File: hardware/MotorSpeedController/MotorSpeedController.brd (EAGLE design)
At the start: 51.2 x 29.2 mm, 49 parts, among them IC1 MIC5219 5V, IC2 ATMEGA32U4-AU, J1 POWER, J2 MOTOR, J3 USB MICRO, J4 I2C, J5 PROG, Q1 16MHz

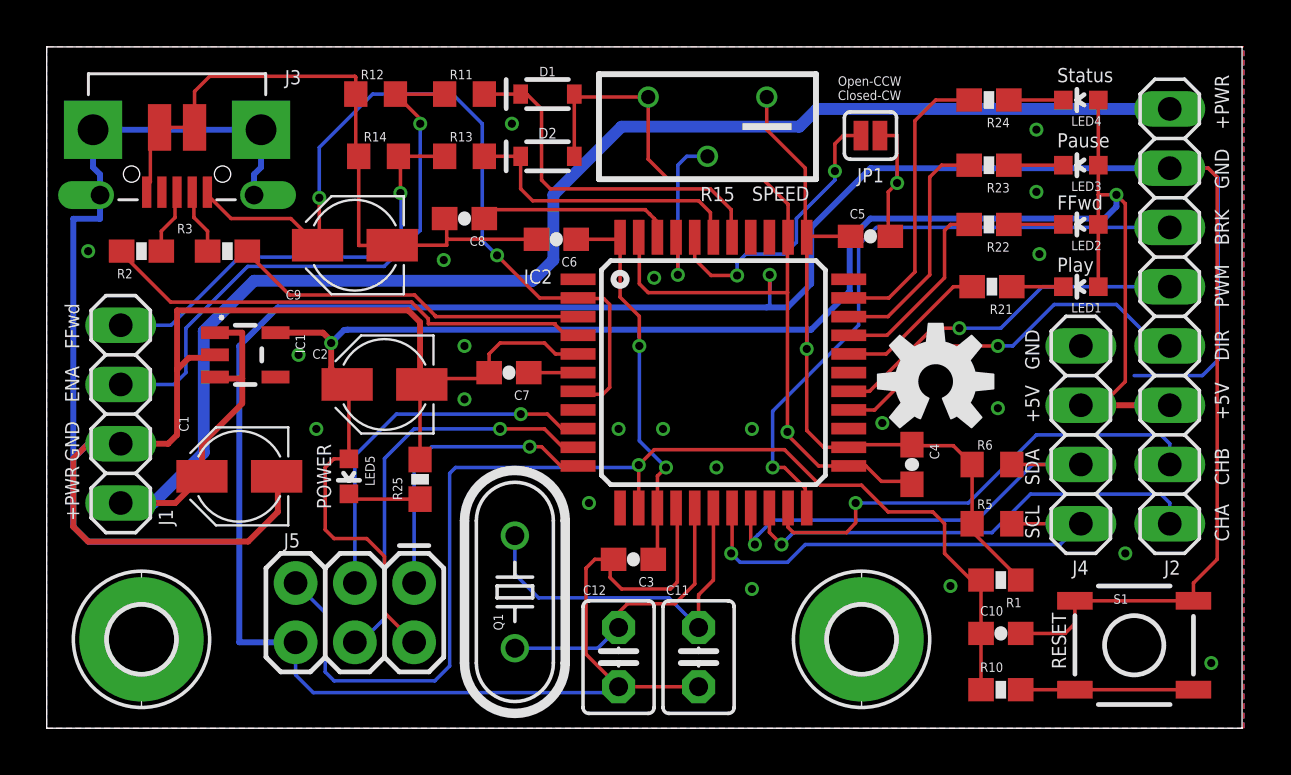
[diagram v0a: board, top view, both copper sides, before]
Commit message: Add I2C interrupt/IO.
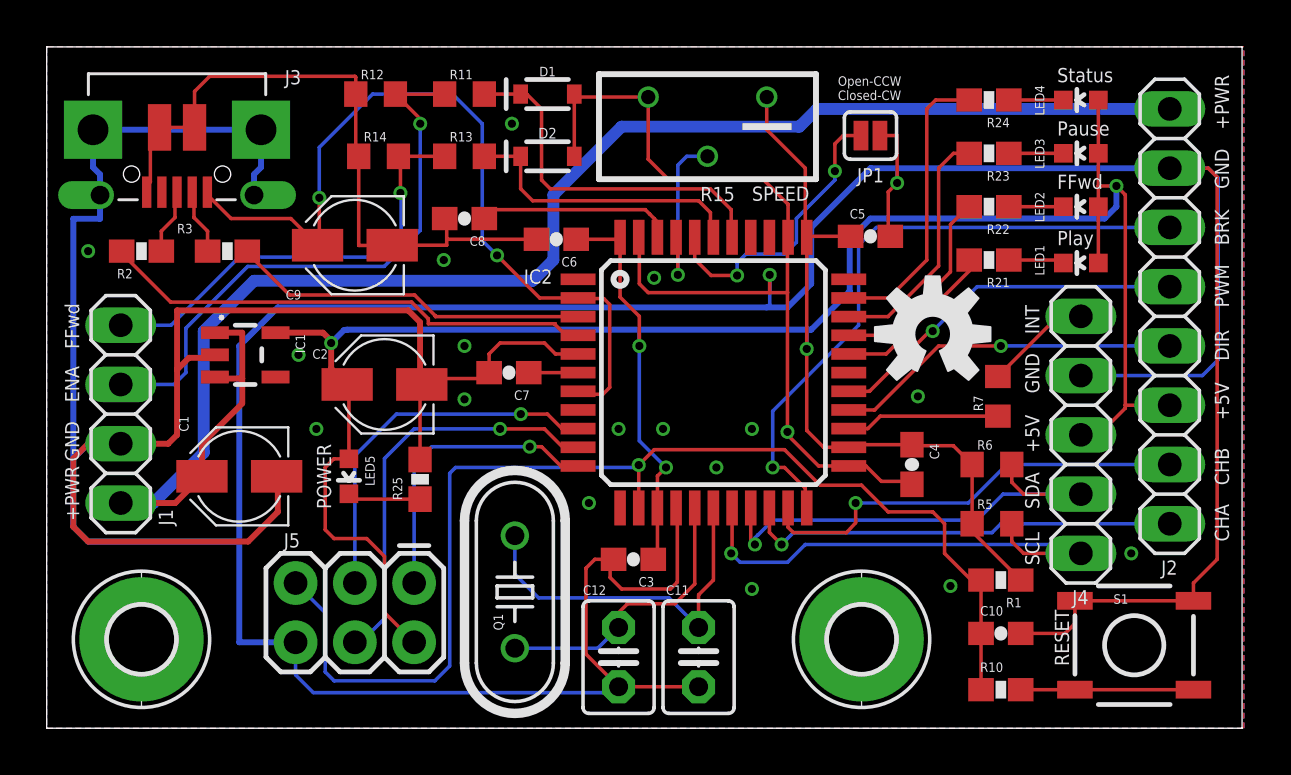
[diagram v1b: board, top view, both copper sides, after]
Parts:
- added R7: 4.7k, rcl:R0603
- J4: device pinhead:1X04 -> pinhead:1X05
- moved U$1 2.04 mm to (38.0, 16.9)
- moved U$2 1.17 mm to (42.9, 1.52)
- moved R21 1.15 mm to (40.4, 20.1)
- moved LED1 1.02 mm to (44.3, 19.9)
- moved LED2 0.76 mm to (44.3, 22.4)
- moved R22 0.76 mm to (40.4, 22.4)
- moved LED3 0.51 mm to (44.3, 24.6)
- moved R23 0.51 mm to (40.4, 24.6)
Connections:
- new net INT: IC2.25, R7.1
- new net N$8: J4.5, R7.2
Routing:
- net INT: track 0.00 -> 6.61 mm
- net N$8: track 0.00 -> 4.62 mm
- net GND: track 303.5 -> 305.2 mm, vias 25 -> 20
- net CHB: track 20.6 -> 19.0 mm
- net CHA: track 20.4 -> 18.8 mm
- net DIR: track 16.4 -> 14.9 mm
- net +5V: track 128.8 -> 127.8 mm
- net SCL: track 20.7 -> 21.5 mm
- net LED1: track 6.48 -> 7.10 mm
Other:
- board text added: "INT"

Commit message: Change footprints to match ordered parts. Put some space between crystal and ICSP. Increase clearance on PWR trace.
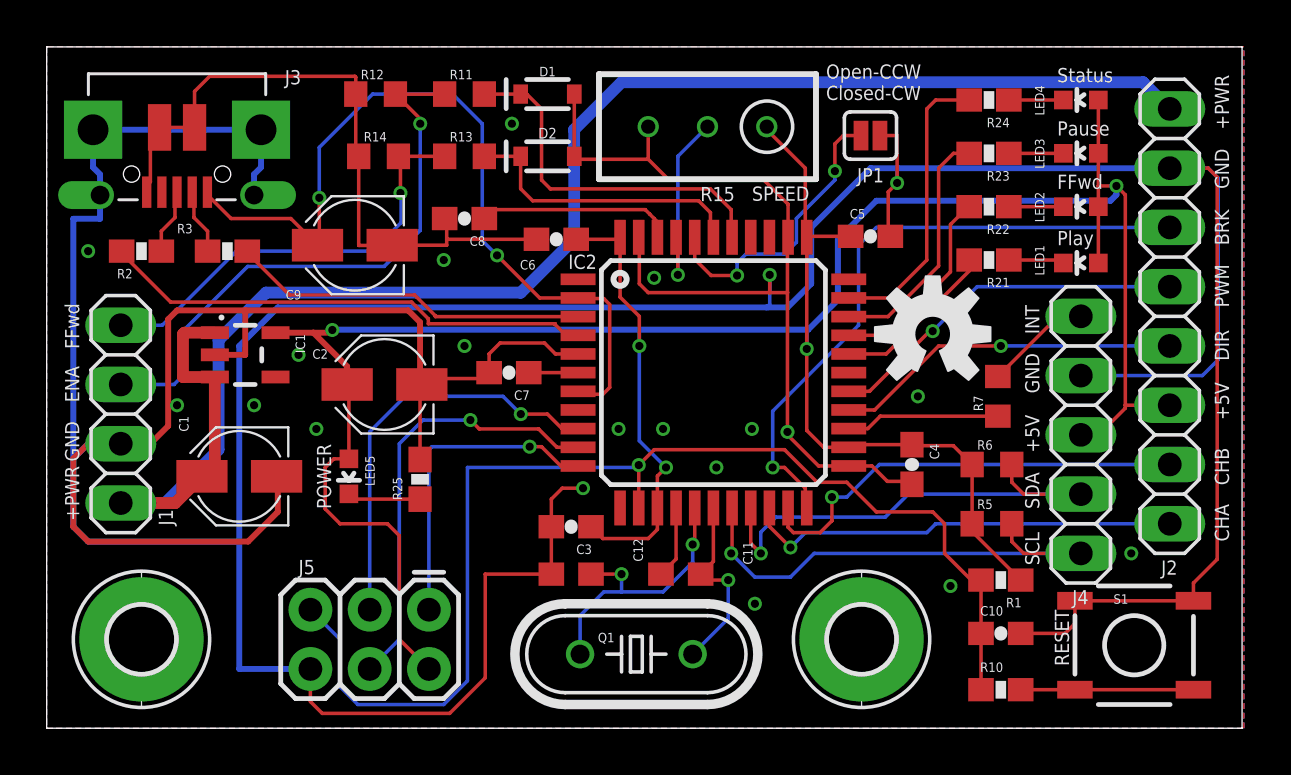
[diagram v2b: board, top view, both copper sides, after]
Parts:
- C11, C12: value 20pF -> 22pF; device adafruit:C025-030X050 -> SparkFun-Capacitors:0603
- R15: device rcl:RTRIM3296Y -> rcl:RTRIM3296W
- moved Q1 5.85 mm to (25.3, 3.17), turned to 0 degrees
- moved C12 4.10 mm to (22.5, 6.60), turned to 180 degrees
- moved C11 3.64 mm to (27.2, 6.60), turned to 180 degrees
- moved C3 3.01 mm to (22.5, 8.64)
- moved U$2 2.82 mm to (40.1, 1.91)
- moved J5 1.31 mm to (16.4, 5.08)
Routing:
- net N$3: track 15.9 -> 8.16 mm, vias 0 -> 1
- net GND: track 305.2 -> 298.2 mm, vias 20 -> 21
- net +5V: track 127.8 -> 130.6 mm
- net CLK: track 16.0 -> 17.8 mm
- net +PWR: track 69.8 -> 71.4 mm
- net MOSI: track 17.7 -> 18.7 mm
- net MISO: track 12.8 -> 13.6 mm
- net SDA: track 20.6 -> 21.4 mm
- net SPEED: track 7.77 -> 8.52 mm
- net N$7: track 12.5 -> 11.9 mm, vias 0 -> 2
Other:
- board text added: "Crazy Giraffe Software"
- board text removed: "by Crazy Giraffe Software"
